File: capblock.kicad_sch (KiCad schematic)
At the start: 32 parts

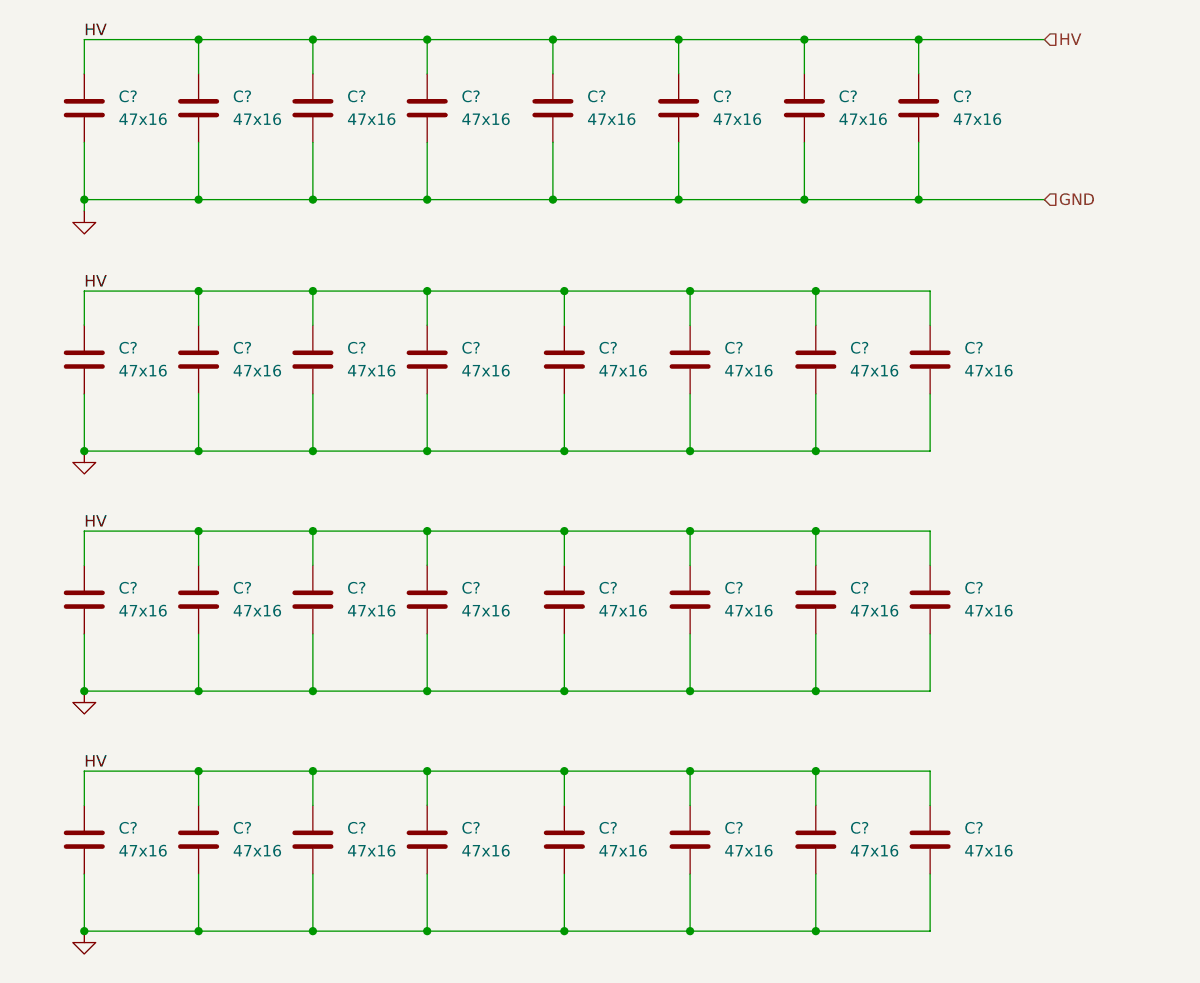
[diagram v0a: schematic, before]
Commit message: Fix capacitor values
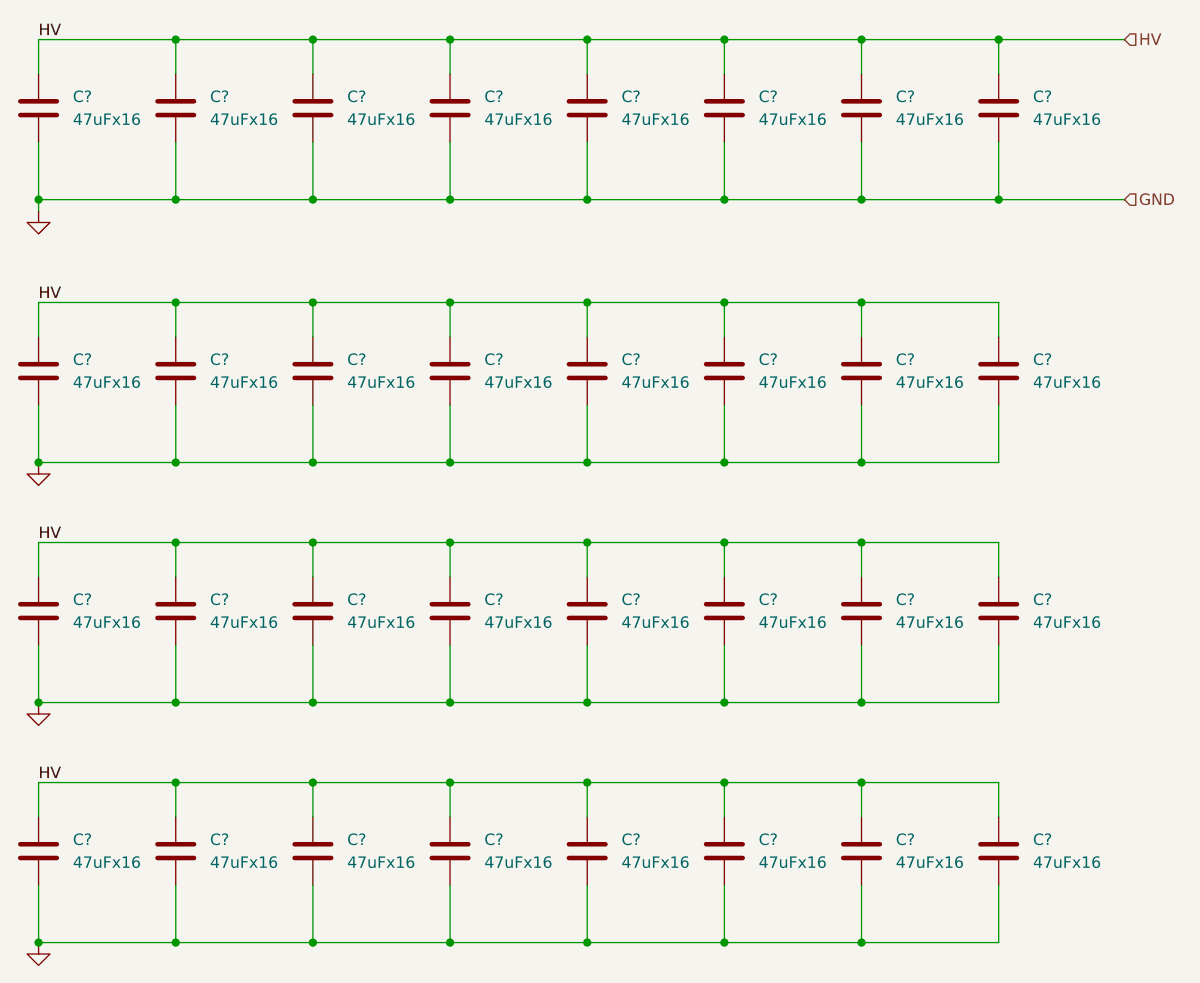
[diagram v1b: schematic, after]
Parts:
- C? (x32): value 47x16 -> 47uFx16
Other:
- moved on the sheet: C?

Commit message: Fill up mouser part numbers
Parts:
- C? (x32): MouserPN (none) -> 581-1210YG474ZAT2A

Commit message: Fix BOM
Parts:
- C? (x32): MouserPN 581-1210YG474ZAT2A -> 80-C1210C476M4P7210
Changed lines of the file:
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@@
 			)
 		)
-		(property "MouserPN" "581-1210YG474ZAT2A "
+		(property "MouserPN" "80-C1210C476M4P7210"
 			(at 95.25 83.82 0)
 			(effects
@@
 			)
 		)
-		(property "MouserPN" "581-1210YG474ZAT2A "
+		(property "MouserPN" "80-C1210C476M4P7210"
 			(at 140.97 110.49 0)
 			(effects
@@
 			)
 		)
-		(property "MouserPN" "581-1210YG474ZAT2A "
+		(property "MouserPN" "80-C1210C476M4P7210"
 			(at 140.97 83.82 0)
 			(effects
@@
 			)
 		)
-		(property "MouserPN" "581-1210YG474ZAT2A "
+		(property "MouserPN" "80-C1210C476M4P7210"
 			(at 186.69 110.49 0)
 			(effects
@@
 			)
 		)
-		(property "MouserPN" "581-1210YG474ZAT2A "
+		(property "MouserPN" "80-C1210C476M4P7210"
 			(at 186.69 137.16 0)
 			(effects
@@
 			)
 		)
-		(property "MouserPN" "581-1210YG474ZAT2A "
+		(property "MouserPN" "80-C1210C476M4P7210"
 			(at 125.73 83.82 0)
 			(effects
@@
 			)
 		)
-		(property "MouserPN" "581-1210YG474ZAT2A "
+		(property "MouserPN" "80-C1210C476M4P7210"
 			(at 95.25 137.16 0)
 			(effects
@@
 			)
 		)
-		(property "MouserPN" "581-1210YG474ZAT2A "
+		(property "MouserPN" "80-C1210C476M4P7210"
 			(at 140.97 137.16 0)
 			(effects
@@
 			)
 		)
-		(property "MouserPN" "581-1210YG474ZAT2A "
+		(property "MouserPN" "80-C1210C476M4P7210"
 			(at 125.73 110.49 0)
 			(effects
@@
 			)
 		)
-		(property "MouserPN" "581-1210YG474ZAT2A "
+		(property "MouserPN" "80-C1210C476M4P7210"
 			(at 171.45 137.16 0)
 			(effects
@@
 			)
 		)
-		(property "MouserPN" "581-1210YG474ZAT2A "
+		(property "MouserPN" "80-C1210C476M4P7210"
 			(at 156.21 110.49 0)
 			(effects
@@
 			)
 		)
-		(property "MouserPN" "581-1210YG474ZAT2A "
+		(property "MouserPN" "80-C1210C476M4P7210"
 			(at 110.49 54.61 0)
 			(effects
@@
 			)
 		)
-		(property "MouserPN" "581-1210YG474ZAT2A "
+		(property "MouserPN" "80-C1210C476M4P7210"
 			(at 201.93 137.16 0)
 			(effects
@@
 			)
 		)
-		(property "MouserPN" "581-1210YG474ZAT2A "
+		(property "MouserPN" "80-C1210C476M4P7210"
 			(at 95.25 54.61 0)
 			(effects
@@
 			)
 		)
-		(property "MouserPN" "581-1210YG474ZAT2A "
+		(property "MouserPN" "80-C1210C476M4P7210"
 			(at 95.25 110.49 0)
 			(effects
@@
 			)
 		)
-		(property "MouserPN" "581-1210YG474ZAT2A "
+		(property "MouserPN" "80-C1210C476M4P7210"
 			(at 201.93 54.61 0)
 			(effects
@@
 			)
 		)
-		(property "MouserPN" "581-1210YG474ZAT2A "
+		(property "MouserPN" "80-C1210C476M4P7210"
 			(at 140.97 54.61 0)
 			(effects
@@
 			)
 		)
-		(property "MouserPN" "581-1210YG474ZAT2A "
+		(property "MouserPN" "80-C1210C476M4P7210"
 			(at 156.21 83.82 0)
 			(effects
@@
 			)
 		)
-		(property "MouserPN" "581-1210YG474ZAT2A "
+		(property "MouserPN" "80-C1210C476M4P7210"
 			(at 156.21 54.61 0)
 			(effects
@@
 			)
 		)
-		(property "MouserPN" "581-1210YG474ZAT2A "
+		(property "MouserPN" "80-C1210C476M4P7210"
 			(at 171.45 83.82 0)
 			(effects
@@
 			)
 		)
-		(property "MouserPN" "581-1210YG474ZAT2A "
+		(property "MouserPN" "80-C1210C476M4P7210"
 			(at 201.93 83.82 0)
 			(effects
@@
 			)
 		)
-		(property "MouserPN" "581-1210YG474ZAT2A "
+		(property "MouserPN" "80-C1210C476M4P7210"
 			(at 110.49 110.49 0)
 			(effects
@@
 			)
 		)
-		(property "MouserPN" "581-1210YG474ZAT2A "
+		(property "MouserPN" "80-C1210C476M4P7210"
 			(at 171.45 54.61 0)
 			(effects
@@
 			)
 		)
-		(property "MouserPN" "581-1210YG474ZAT2A "
+		(property "MouserPN" "80-C1210C476M4P7210"
 			(at 156.21 137.16 0)
 			(effects
@@
 			)
 		)
-		(property "MouserPN" "581-1210YG474ZAT2A "
+		(property "MouserPN" "80-C1210C476M4P7210"
 			(at 186.69 83.82 0)
 			(effects
@@
 			)
 		)
-		(property "MouserPN" "581-1210YG474ZAT2A "
+		(property "MouserPN" "80-C1210C476M4P7210"
 			(at 125.73 137.16 0)
 			(effects
@@
 			)
 		)
-		(property "MouserPN" "581-1210YG474ZAT2A "
+		(property "MouserPN" "80-C1210C476M4P7210"
 			(at 110.49 83.82 0)
 			(effects
@@
 			)
 		)
-		(property "MouserPN" "581-1210YG474ZAT2A "
+		(property "MouserPN" "80-C1210C476M4P7210"
 			(at 171.45 110.49 0)
 			(effects
@@
 			)
 		)
-		(property "MouserPN" "581-1210YG474ZAT2A "
+		(property "MouserPN" "80-C1210C476M4P7210"
 			(at 110.49 137.16 0)
 			(effects
@@
 			)
 		)
-		(property "MouserPN" "581-1210YG474ZAT2A "
+		(property "MouserPN" "80-C1210C476M4P7210"
 			(at 201.93 110.49 0)
 			(effects
@@
 			)
 		)
-		(property "MouserPN" "581-1210YG474ZAT2A "
+		(property "MouserPN" "80-C1210C476M4P7210"
 			(at 186.69 54.61 0)
 			(effects
@@
 			)
 		)
-		(property "MouserPN" "581-1210YG474ZAT2A "
+		(property "MouserPN" "80-C1210C476M4P7210"
 			(at 125.73 54.61 0)
 			(effects
